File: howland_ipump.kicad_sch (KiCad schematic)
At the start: 13 parts

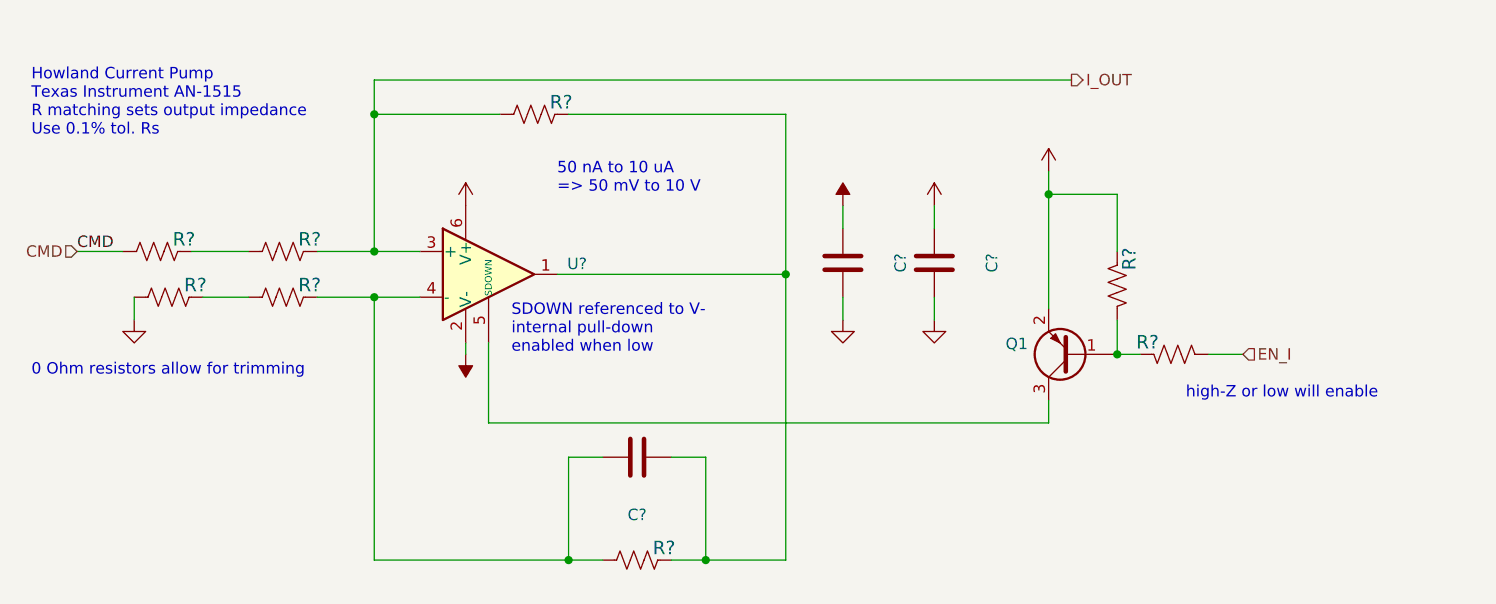
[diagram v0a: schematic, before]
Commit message: closes #31 - incorrect text on Howland current pump. Also, updated fast DAC symbol but not closing until layout is corrected
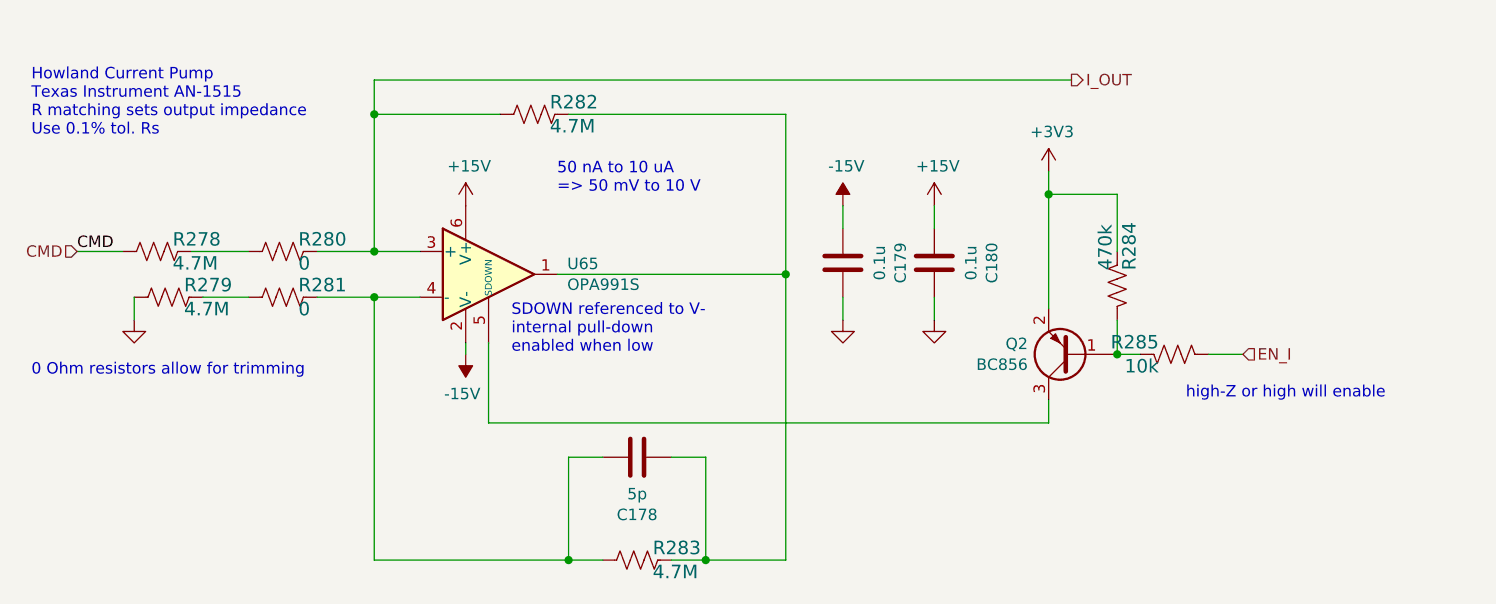
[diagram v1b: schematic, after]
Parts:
- C178: renamed from C?; value (none) -> 5p; footprint (none) -> Capacitor_SMD:C_0603_1608Metric
- C179, C180: renamed from C?; value (none) -> 0.1u; footprint (none) -> Capacitor_SMD:C_0603_1608Metric
- Q2: renamed from Q1; value (none) -> BC856; footprint (none) -> Package_TO_SOT_SMD:SOT-23
- R278, R279, R282, R283: renamed from R?; value (none) -> 4.7M; footprint (none) -> Resistor_SMD:R_1206_3216Metric
- R280, R281: renamed from R?; value (none) -> 0; footprint (none) -> Resistor_SMD:R_0603_1608Metric
- R284: renamed from R?; value (none) -> 470k; footprint (none) -> Resistor_SMD:R_0603_1608Metric
- R285: renamed from R?; value (none) -> 10k; footprint (none) -> Resistor_SMD:R_0603_1608Metric
- U65: renamed from U?; value (none) -> OPA991S; footprint (none) -> Package_TO_SOT_SMD:SOT-23-6
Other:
- note added: "high-Z or high will enable"
- note removed: "high-Z or low will enable"

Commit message: Closes #29 full-scale range will be nearly 8uA
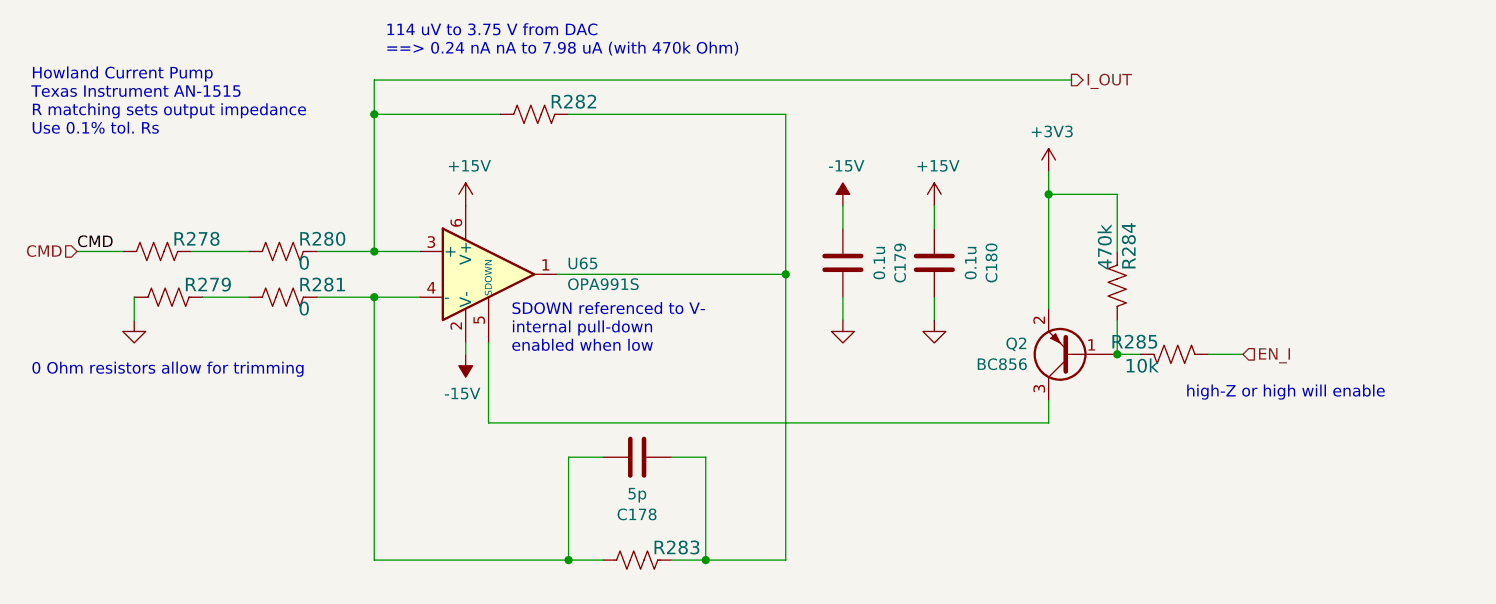
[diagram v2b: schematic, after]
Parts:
- R278, R279, R282, R283: value 4.7M -> (none); footprint Resistor_SMD:R_1206_3216Metric -> (none); Manf# RG3216P-4704-B-T1 -> RG3216P-4703-B-T1
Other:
- note added: "114 uV to 3.75 V from DAC ==> 0.24 nA nA to 7.98 uA (with 470k Ohm)"
- note removed: "50 nA to 10 uA => 50 mV to 10 V"
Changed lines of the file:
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@@
     (effects (font (size 1.27 1.27)) (justify left bottom))
   )
-  (text "50 nA to 10 uA\n=> 50 mV to 10 V " (at 139.7 85.09 0)
+  (text "114 uV to 3.75 V from DAC \n==> 0.24 nA nA to 7.98 uA (with 470k Ohm)\n"
+    (at 120.65 69.85 0)
     (effects (font (size 1.27 1.27)) (justify left bottom))
   )
@@
       (effects (font (size 1.4986 1.4986)) (justify left))
     )
-    (property "Value" "4.7M" (id 1) (at 98.2472 97.8408 90)
-      (effects (font (size 1.4986 1.4986)) (justify left))
-    )
-    (property "Footprint" "Resistor_SMD:R_1206_3216Metric" (id 2) (at 96.52 96.52 0)
+    (property "Value" "" (id 1) (at 98.2472 97.8408 90)
+      (effects (font (size 1.4986 1.4986)) (justify left))
+    )
+    (property "Footprint" "" (id 2) (at 96.52 96.52 0)
       (effects (font (size 1.27 1.27)) hide)
     )
@@
       (effects (font (size 1.27 1.27)) hide)
     )
-    (property "Manf#" "RG3216P-4704-B-T1" (id 4) (at 100.7872 95.1738 0)
+    (property "Manf#" "RG3216P-4703-B-T1" (id 4) (at 100.7872 95.1738 0)
       (effects (font (size 1.27 1.27)) hide)
     )
@@
       (effects (font (size 1.4986 1.4986)) (justify left))
     )
-    (property "Value" "4.7M" (id 1) (at 96.9772 92.7608 90)
-      (effects (font (size 1.4986 1.4986)) (justify left))
-    )
-    (property "Footprint" "Resistor_SMD:R_1206_3216Metric" (id 2) (at 95.25 91.44 0)
+    (property "Value" "" (id 1) (at 96.9772 92.7608 90)
+      (effects (font (size 1.4986 1.4986)) (justify left))
+    )
+    (property "Footprint" "" (id 2) (at 95.25 91.44 0)
       (effects (font (size 1.27 1.27)) hide)
     )
@@
       (effects (font (size 1.27 1.27)) hide)
     )
-    (property "Manf#" "RG3216P-4704-B-T1" (id 4) (at 99.5172 90.0938 0)
+    (property "Manf#" "RG3216P-4703-B-T1" (id 4) (at 99.5172 90.0938 0)
       (effects (font (size 1.27 1.27)) hide)
     )
@@
       (effects (font (size 1.4986 1.4986)) (justify left))
     )
-    (property "Value" "4.7M" (id 1) (at 138.8872 77.5208 90)
-      (effects (font (size 1.4986 1.4986)) (justify left))
-    )
-    (property "Footprint" "Resistor_SMD:R_1206_3216Metric" (id 2) (at 137.16 76.2 0)
+    (property "Value" "" (id 1) (at 138.8872 77.5208 90)
+      (effects (font (size 1.4986 1.4986)) (justify left))
+    )
+    (property "Footprint" "" (id 2) (at 137.16 76.2 0)
       (effects (font (size 1.27 1.27)) hide)
     )
@@
       (effects (font (size 1.27 1.27)) hide)
     )
-    (property "Manf#" "RG3216P-4704-B-T1" (id 4) (at 141.4272 74.8538 0)
+    (property "Manf#" "RG3216P-4703-B-T1" (id 4) (at 141.4272 74.8538 0)
       (effects (font (size 1.27 1.27)) hide)
     )
@@
       (effects (font (size 1.4986 1.4986)) (justify left))
     )
-    (property "Value" "4.7M" (id 1) (at 150.3172 127.0508 90)
-      (effects (font (size 1.4986 1.4986)) (justify left))
-    )
-    (property "Footprint" "Resistor_SMD:R_1206_3216Metric" (id 2) (at 148.59 125.73 0)
+    (property "Value" "" (id 1) (at 150.3172 127.0508 90)
+      (effects (font (size 1.4986 1.4986)) (justify left))
+    )
+    (property "Footprint" "" (id 2) (at 148.59 125.73 0)
       (effects (font (size 1.27 1.27)) hide)
     )
@@
       (effects (font (size 1.27 1.27)) hide)
     )
-    (property "Manf#" "RG3216P-4704-B-T1" (id 4) (at 152.8572 124.3838 0)
-      (effects (font (size 1.27 1.27)) hide)
-    )
+    (property "Manf#" "RG3216P-4703-B-T1" (id 4) (at 152.8572 124.3838 0)
+      (effects (font (size 1.27 1.27)) hide)
+    )
